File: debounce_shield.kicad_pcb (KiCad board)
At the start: 2 copper layers, 65 x 56 mm, 65 parts, among them J1 Conn_01x06, J2 RPi_GPIO, J3 Conn_01x06, J4 Conn_01x06, J5 Conn_01x02, P2 CONN_2, U1 74LVT04, U2 CAT24C32, U3 LTV-824, U4 LTV-824, U5 LTV-824

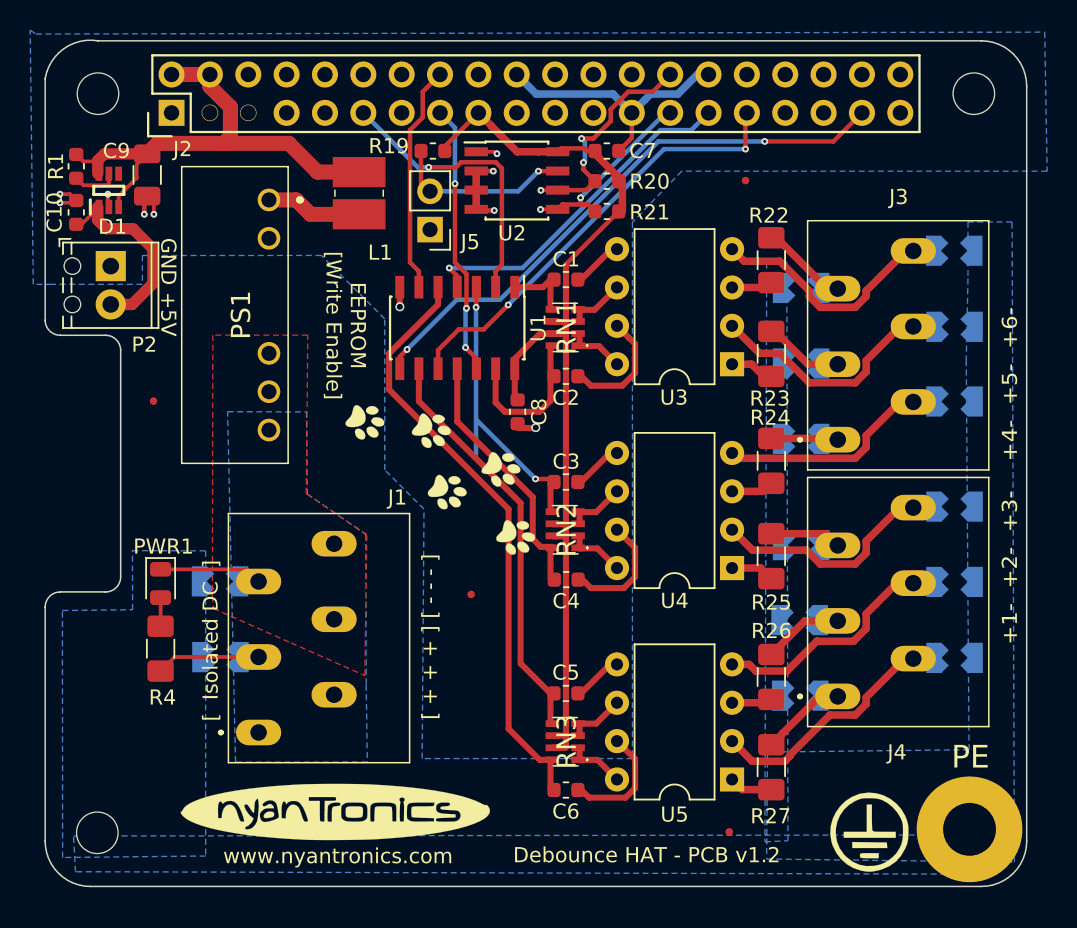
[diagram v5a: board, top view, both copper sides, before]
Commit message: Update schematic & PCB with new terminal connectors.
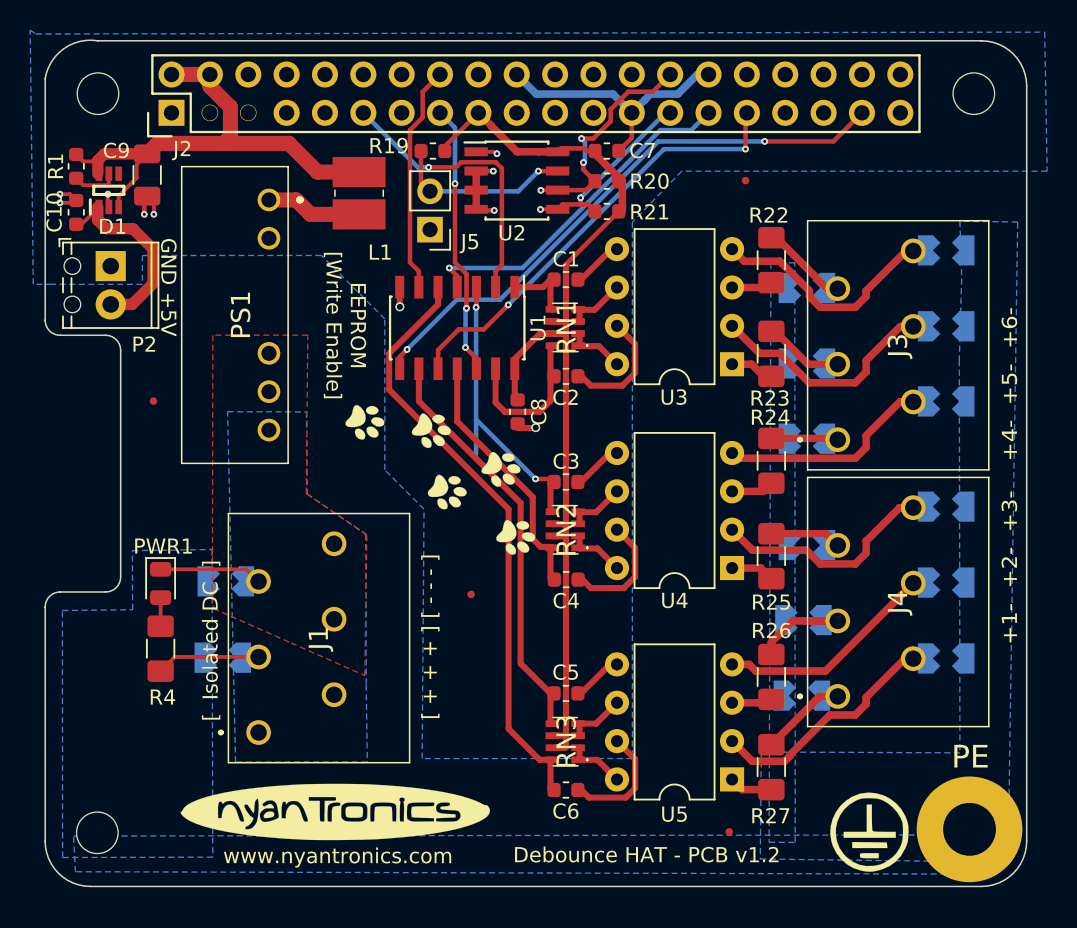
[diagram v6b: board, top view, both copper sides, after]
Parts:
- J1, J3, J4: footprint SamacSys_Parts:GSL002C25006P -> GSL002C-2.50-06P:GSL002C25006P
- U1: value 74LVT04 -> 74LV14D
- moved E11 0.56 mm to (157.2, 108.5)
- moved E13 0.56 mm to (157.2, 113.5)
- moved E5 0.56 mm to (157.2, 91.5)
- moved E9 0.56 mm to (157.2, 103.4)
- moved E7 0.56 mm to (157.2, 96.5)
- moved E3 0.53 mm to (157.2, 86.5)
- moved E8 0.38 mm to (148.0, 98.9)
- moved E10 0.38 mm to (148.0, 106.0)
- moved E2 0.38 mm to (109.5, 108.4)
- moved E4 0.38 mm to (148.0, 89.0)
- moved E6 0.38 mm to (148.0, 94.0)
- moved E12 0.25 mm to (147.7, 110.9)
- moved E1 0.16 mm to (109.3, 113.4)
- moved E14 0.11 mm to (147.6, 116.0)
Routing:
- net Net-(E12-Pad2): track 5.32 -> 8.90 mm
- net Net-(E14-Pad2): track 6.06 -> 7.09 mm
- net Net-(E1-Pad2): track 6.88 -> 7.90 mm
- net Net-(E13-Pad2): track 15.7 -> 16.5 mm
- net Net-(E11-Pad2): track 15.2 -> 14.6 mm

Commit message: Change 6-position terminal to fixed Phoenix Contact 1990041 footprint.
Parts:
- J1, J3, J4: footprint GSL002C-2.50-06P:GSL002C25006P -> Phoenix_Contact_1990041:1990041
- moved J4 13.5 mm to (155.0, 103.5)
- moved J3 13.5 mm to (155.1, 86.5)
- moved J1 13.5 mm to (116.7, 105.9)
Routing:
- net Net-(E4-Pad2): track 5.80 -> 7.39 mm
- net Net-(E6-Pad2): track 5.30 -> 6.75 mm
- net Net-(E8-Pad2): track 4.44 -> 5.87 mm
- net Net-(E2-Pad2): track 6.82 -> 7.68 mm
- net Net-(E9-Pad2): track 15.0 -> 15.7 mm
- net Net-(E11-Pad2): track 14.6 -> 15.4 mm

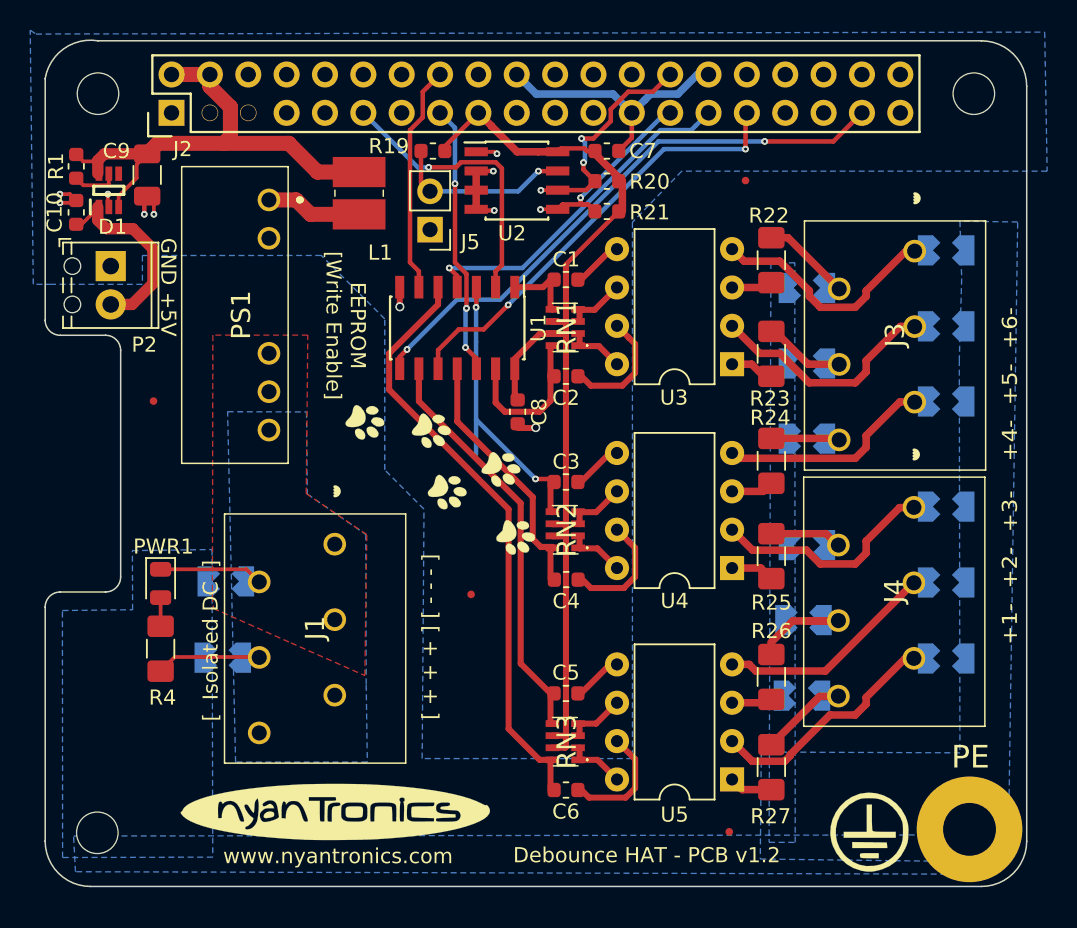
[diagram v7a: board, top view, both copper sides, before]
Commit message: Update to v1.2-beta PCB revision.
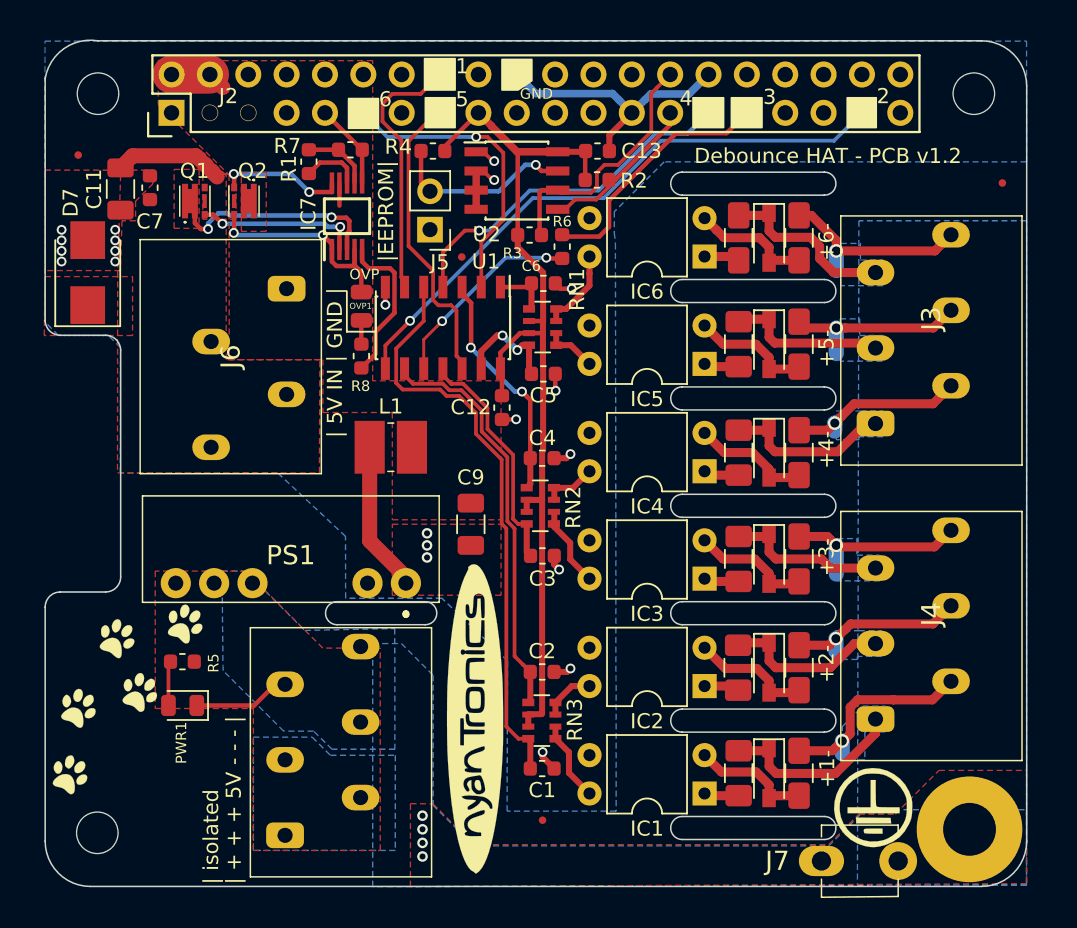
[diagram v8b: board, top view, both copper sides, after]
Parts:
- removed C10: 100 nF, Capacitor_SMD:C_0603_1608Metric
- removed E1, E10, E11, E12, E13, E14, E2, E3, E4, E5, E6, E7, E8, E9: SPARK_GAP, libs:SG1210
- removed P2: CONN_2, TerminalBlock_Phoenix:TerminalBlock_Phoenix_MPT-0,5-2-2.54_1x02_P2.54mm_Horizontal
- removed the R22 at (145.6, 87.1)
- removed the R4 at (105.2, 112.8)
- removed U3, U4, U5: LTV-824, Package_DIP:DIP-8_W7.62mm
- added C11: 10uF, Capacitor_SMD:C_1206_3216Metric, F.Cu at (102.5, 82.4)
- added C13: 100 nF, Capacitor_SMD:C_0603_1608Metric, F.Cu at (134.1, 79.9)
- added D2: D_TVS, Diode_SMD:D_SOD-123, F.Cu at (145.4, 114.1)
- added D3: D_TVS, Diode_SMD:D_SOD-123, F.Cu at (145.4, 106.9)
- added D4: D_TVS, Diode_SMD:D_SOD-123, F.Cu at (145.4, 99.9)
- added D5: D_TVS, Diode_SMD:D_SOD-123, F.Cu at (145.4, 92.7)
- added D6: D_TVS, Diode_SMD:D_SOD-123, F.Cu at (145.4, 85.6)
- added D7: D_TVS, Diode_SMD:D_SMB, F.Cu at (100.3, 87.9)
- added IC1: LTV-814, Package_DIP:DIP-4_W7.62mm, F.Cu at (141.2, 122.4)
- added IC2: LTV-814, Package_DIP:DIP-4_W7.62mm, F.Cu at (141.2, 115.3)
- added IC3: LTV-814, Package_DIP:DIP-4_W7.62mm, F.Cu at (141.2, 108.2)
- added IC4: LTV-814, Package_DIP:DIP-4_W7.62mm, F.Cu at (141.2, 101.1)
- added IC5: LTV-814, Package_DIP:DIP-4_W7.62mm, F.Cu at (141.2, 94.0)
- added IC6: LTV-814, Package_DIP:DIP-4_W7.62mm, F.Cu at (141.2, 86.9)
- added IC7: MAX16914AUB+, MAX16914AUB+:SOP50P490X110-10N, F.Cu at (117.5, 84.2)
- added J6: 1985218, Phoenix_Contact_1985218:1985218, F.Cu at (113.5, 89.0)
- added J7: 1285, Keystone_1285:1285, F.Cu at (151.5, 126.9)
- added OVP1: LED, LED_SMD:LED_0805_2012Metric, F.Cu at (118.5, 90.2)
- added Q1: DMP3028LFDE7, DMP2066UFDE7:U-DFN2020-6, F.Cu at (107.4, 83.2)
- added Q2: DMP3028LFDE7, DMP2066UFDE7:U-DFN2020-6, F.Cu at (110.7, 83.2)
- added R11: 1k, Resistor_SMD:R_1206_3216Metric_Pad1.42x1.75mm_HandSolder, F.Cu at (147.4, 121.1)
- added R12: 1k, Resistor_SMD:R_1206_3216Metric_Pad1.42x1.75mm_HandSolder, F.Cu at (147.4, 114.1)
- added R13: 1k, Resistor_SMD:R_1206_3216Metric_Pad1.42x1.75mm_HandSolder, F.Cu at (147.4, 106.9)
- added R14: 1k, Resistor_SMD:R_1206_3216Metric_Pad1.42x1.75mm_HandSolder, F.Cu at (147.4, 99.9)
- added R15: 1k, Resistor_SMD:R_1206_3216Metric_Pad1.42x1.75mm_HandSolder, F.Cu at (147.4, 92.7)
- added R16: 1k, Resistor_SMD:R_1206_3216Metric_Pad1.42x1.75mm_HandSolder, F.Cu at (147.4, 85.6)
- added R26: 1k, Resistor_SMD:R_1206_3216Metric_Pad1.42x1.75mm_HandSolder, F.Cu at (143.4, 85.6)
- added R5: 1k, Resistor_SMD:R_0603_1608Metric, F.Cu at (106.6, 113.7)
- added R6: 1k, Resistor_SMD:R_0603_1608Metric, F.Cu at (131.8, 86.2)
- added R7: 1k, Resistor_SMD:R_0603_1608Metric, F.Cu at (117.7, 79.8)
- added R8: 3.9k, Resistor_SMD:R_0603_1608Metric, F.Cu at (118.5, 93.5)
- C1: renamed from C6; value 100n -> 100 nF
- C12: renamed from C8; value 100n -> 100 nF
- C2: renamed from C5; value 100n -> 100 nF
- C3: renamed from C4; value 100n -> 100 nF
- C4: renamed from C3; value 100n -> 100 nF
- C5: renamed from C2; value 100n -> 100 nF
- C6: renamed from C1; value 100n -> 100 nF
- C7: value 100n -> 100 nF
- D1: value LM66100DCKR -> D_TVS; footprint LM66100DCKR:SOP65P210X110-6N -> Diode_SMD:D_SOD-123
- R1: value 10k 1% -> 3.9k
- R21: renamed from R27; value 1.2k -> 1k
- R22: renamed from R26; value 1.2k -> 1k
- R23: renamed from R25; value 1.2k -> 1k
- R24: value 1.2k -> 1k
- R25: renamed from R23; value 1.2k -> 1k
- RN1, RN2, RN3: value YC164-JR-07100RL -> R_Pack04; footprint YC164-JR-07100RL:YC164JR07220RL -> Resistor_SMD:R_Array_Convex_4x0603
- moved D1 58.3 mm to (145.4, 121.1), turned to 270 degrees
- moved C9 31.5 mm to (125.7, 104.6), turned to 90 degrees
- moved C7 30.4 mm to (104.5, 82.3), turned to 90 degrees
- moved PS1 27.0 mm to (121.4, 108.5), turned to 180 degrees
- moved G*** 25.3 mm to (103.0, 116.2), turned to 0 degrees
- moved REF** 22.4 mm to (125.1, 86.9)
- moved REF** 17.0 mm to (99.7, 80.2)
- moved REF** 17.0 mm to (160.9, 82.0)
- moved L1 17.0 mm to (120.4, 99.5), turned to 180 degrees
- moved R1 15.4 mm to (115.0, 80.6)
- moved REF** 12.4 mm to (130.4, 124.2)
- moved G*** 11.0 mm to (125.9, 117.5), turned to 90 degrees
- moved PWR1 8.21 mm to (106.6, 116.6), turned to 180 degrees
- moved J1 6.99 mm to (118.4, 112.7)
- moved R3 5.35 mm to (129.6, 85.4)
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- renumbered R20 to R2, R21 to R3, R19 to R4
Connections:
- C7 pad 1: GND -> /+5V_in
- C7 pad 2: +3.3V -> GND
- C9 pad 1: +5V -> GND
- C9 pad 2: GND -> +5V
- D1 pad 1: /+5V_in -> Net-(D1-Pad1)
- D1 pad 2: GND -> Net-(D1-Pad2)
- J4 pad 1: Net-(E14-Pad2) -> Net-(D1-Pad1)
- R1 pad 1: +5V -> Net-(IC7-Pad7)
- R1 pad 2: Net-(D1-Pad5) -> Net-(IC7-Pad8)
- R2 pad 2: IDSCL -> IDSDA
- R21 pad 2: Net-(E14-Pad2) -> Net-(D1-Pad1)
- R3 pad 1: IDSDA -> +3.3V
- R3 pad 2: +3.3V -> IDSCL
- U1 pad 10: Net-(J2-Pad31) -> Net-(R6-Pad2)
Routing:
- net +5V: track 33.8 -> 5.26 mm
- net GND: track 65.2 -> 40.1 mm, vias 10 -> 21
- net Net-(C11-Pad1): track 0.00 -> 21.1 mm, vias 0 -> 2
- net Net-(R6-Pad2): track 0.00 -> 13.4 mm, vias 0 -> 2
- net Net-(J2-Pad31): track 29.5 -> 16.8 mm, vias 2 -> 0
- net Net-(D1-Pad1): track 0.00 -> 12.6 mm
- net Net-(IC7-Pad2): track 0.00 -> 10.8 mm, vias 0 -> 2
- net Net-(IC7-Pad5): track 0.00 -> 10.5 mm
- net Net-(IC7-Pad10): track 0.00 -> 8.51 mm, vias 0 -> 2
- net Net-(D6-Pad2): track 0.00 -> 8.16 mm
- net Net-(D2-Pad2): track 0.00 -> 8.03 mm
- net Net-(D1-Pad2): track 0.00 -> 8.02 mm
- net Net-(D5-Pad2): track 0.00 -> 7.97 mm
- net Net-(D3-Pad2): track 0.00 -> 7.93 mm
- net Net-(J1-Pad1): track 7.90 -> 0.00 mm
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- added copper zone on F.Cu, net +5V
- added copper zone on F.Cu, net /+5V_in
- added copper zone on F.Cu, net GND
- added copper zone on F.Cu, net Net-(C11-Pad1)
- added copper zone on B.Cu, net Net-(D1-Pad1)
- added copper zone on B.Cu, net Net-(D2-Pad1)
- added copper zone on B.Cu, net Net-(D3-Pad1)
- added copper zone on B.Cu, net Net-(D4-Pad1)
- added copper zone on B.Cu, net Net-(D5-Pad1)
- added copper zone on B.Cu, net Net-(D6-Pad1)
- added copper zone on F.Cu, net Net-(J1-Pad1)
- added copper zone on B.Cu, net Net-(J1-Pad4)
- added copper zone on F.Cu, net PE
- removed copper zone on F.Cu, net Net-(J1-Pad4)
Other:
- outline, holes or cut-outs redrawn
- net class Default: via_dia 0.45 -> 0.65; via_drill 0.2 -> 0.4
- board text added: "+1-"
- board text added: "+2-"
- board text added: "+3-"
- board text added: "+4-"
- board text added: "+5-"
- board text added: "+6-"
- board text added: "1"
- board text added: "2"
- board text added: "3"
- board text added: "4"
- board text added: "5"
- board text added: "6"
- board text added: "GND"
- board text added: "OVP"
- board text added: "| + + + 5V - - - |"
- board text added: "| 5V IN | GND |"
- board text added: "| isolated"
- board text added: "|EEPROM|"
- board text removed: "+1- +2- +3- +4- +5- +6-"
- board text removed: "EEPROM [Write Enable]"
- board text removed: "GND +5V"
- board text removed: "[ + + + ] [ - - - ]"
- board text removed: "[ Isolated DC ]"
